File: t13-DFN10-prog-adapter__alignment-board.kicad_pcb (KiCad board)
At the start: 2 copper layers, 13.2 x 16.8 mm, 21 parts, among them P3 DFN10

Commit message: Tweaks.
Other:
- board text added: "V0.10.b"
- board text added: "X"
- board text added: "t13-DFN10 P.A."
- board text removed: "ATtiny13"
- board text removed: "DFN10"
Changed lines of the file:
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@@
-(kicad_pcb (version 3) (host pcbnew "(2014-03-16 BZR 4752)-product")
+(kicad_pcb (version 3) (host pcbnew "(2014-03-14 BZR 4750)-product")
   (general
     (links 0)
@@
     (area 139.15099 91.5068 153.96501 110.7312)
     (thickness 1.6)
-    (drawings 13)
+    (drawings 14)
     (tracks 0)
     (zones 0)
@@
   (page A4)
   (title_block
-    (title "ATtiny13 DFN10 programming adapter")
+    (title "ATtiny13 DFN10 programming adapter - alignment board")
     (date "17 Mar 2014")
-    (rev 0.10.a)
+    (rev 0.10.b)
     (company "2014 - blog.spitzenpfeil.org")
   )
@@
     (mod_text_size 1 1)
     (mod_text_width 0.15)
-    (pad_size 0.3302 0.3302)
-    (pad_drill 0.3302)
+    (pad_size 1.65 1.65)
+    (pad_drill 0.6)
     (pad_to_mask_clearance 0)
     (aux_axis_origin 0 0)
@@
       (effects (font (size 1 1) (thickness 0.2)))
     )
-    (pad 1 thru_hole rect (at 0 0) (size 1.65 1.65) (drill 0.508) (layers *.Cu *.Mask F.SilkS))
+    (pad 1 thru_hole rect (at 0 0) (size 1.65 1.65) (drill 0.6) (layers *.Cu *.Mask F.SilkS))
   )
   (module my_parts:MADW__SIL-1 (layer F.Cu)
@@
       (effects (font (size 1 1) (thickness 0.2)))
     )
-    (pad 1 thru_hole rect (at 0 0) (size 1.65 1.65) (drill 0.508) (layers *.Cu *.Mask F.SilkS))
+    (pad 1 thru_hole rect (at 0 0) (size 1.65 1.65) (drill 0.6) (layers *.Cu *.Mask F.SilkS))
   )
   (module my_parts:MADW__SIL-1 (layer F.Cu)
@@
       (effects (font (size 1 1) (thickness 0.2)))
     )
-    (pad 1 thru_hole rect (at 0 0) (size 1.65 1.65) (drill 0.508) (layers *.Cu *.Mask F.SilkS))
+    (pad 1 thru_hole rect (at 0 0) (size 1.65 1.65) (drill 0.6) (layers *.Cu *.Mask F.SilkS))
   )
   (module my_parts:MADW__SIL-1 (layer F.Cu)
@@
     (fp_line (start 1.27 -1.27) (end 1.27 1.27) (layer F.SilkS) (width 0.2))
     (fp_line (start -1.27 1.27) (end -1.27 -1.27) (layer F.SilkS) (width 0.2))
-    (pad 1 thru_hole rect (at 0 0) (size 1.65 1.65) (drill 0.508) (layers *.Cu *.Mask F.SilkS))
+    (pad 1 thru_hole rect (at 0 0) (size 1.65 1.65) (drill 0.6) (layers *.Cu *.Mask F.SilkS))
+  )
+  (gr_text X (at 146.6 101.2) (layer F.SilkS)
+    (effects (font (size 1.2 1.2) (thickness 0.3)) (justify mirror))
+  )
+  (gr_text V0.10.b (at 146.6 105.2) (layer F.SilkS)
+    (effects (font (size 1 1) (thickness 0.25)))
   )
   (gr_text 10...6 (at 146.4056 94.742) (layer F.SilkS)
@@
   (gr_line (start 153.162 92.71) (end 153.162 109.474) (angle 90) (layer Edge.Cuts) (width 0.1))
   (gr_line (start 139.954 92.71) (end 153.162 92.71) (angle 90) (layer Edge.Cuts) (width 0.1))
-  (gr_text DFN10 (at 146.5834 104.775) (layer F.SilkS)
-    (effects (font (size 1.2 1.2) (thickness 0.25)))
-  )
-  (gr_text ATtiny13 (at 146.558 97.7646) (layer F.SilkS)
-    (effects (font (size 1.2 1.2) (thickness 0.25)))
+  (gr_text "t13-DFN10 P.A." (at 146.6 97.4) (layer F.SilkS)
+    (effects (font (size 1 1) (thickness 0.25)))
   )
   (gr_line (start 140.208 92.964) (end 152.908 92.964) (angle 90) (layer F.SilkS) (width 0.2))

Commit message: Tweaks.
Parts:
- removed the P? at (145.9, 102.2)
- removed the P? at (147.2, 102.2)
- removed the P? at (146.6, 102.2)
- removed the P? at (146.6, 100.0)
- removed the P? at (147.2, 100.0)
- removed the P? at (145.9, 100.0)
- removed the P? at (145.5, 101.8)
- removed the P? at (145.5, 100.4)
- removed the P? at (145.5, 101.1)
- removed the P? at (147.7, 101.1)
- removed the P? at (147.7, 100.4)
- removed the P? at (147.7, 101.8)
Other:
- outline, holes or cut-outs redrawn
- board text removed: "X"
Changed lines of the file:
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@@
     (area 139.15099 91.5068 153.96501 110.7312)
     (thickness 1.6)
-    (drawings 14)
+    (drawings 22)
     (tracks 0)
     (zones 0)
-    (modules 21)
+    (modules 9)
     (nets 1)
   )
@@
   )
   (module my_parts:MADW__SIL-1 (layer F.Cu)
-    (at 145.4658 101.7778 90)
-    (descr "Connecteurs 2 pins")
-    (tags "CONN DEV")
-    (fp_text reference P? (at 0 -2.032 90) (layer F.SilkS) hide
-      (effects (font (size 1 1) (thickness 0.2)))
-    )
-    (fp_text value VAL** (at 0 2.286 90) (layer F.SilkS) hide
-      (effects (font (size 1 1) (thickness 0.2)))
-    )
-    (pad "" np_thru_hole circle (at 0 0 90) (size 0.3302 0.3302) (drill 0.3302) (layers *.Cu *.Mask F.SilkS))
-  )
-  (module my_parts:MADW__SIL-1 (layer F.Cu)
-    (at 145.4658 100.4062 90)
-    (descr "Connecteurs 2 pins")
-    (tags "CONN DEV")
-    (fp_text reference P? (at 0 -2.032 90) (layer F.SilkS) hide
-      (effects (font (size 1 1) (thickness 0.2)))
-    )
-    (fp_text value VAL** (at 0 2.286 90) (layer F.SilkS) hide
-      (effects (font (size 1 1) (thickness 0.2)))
-    )
-    (pad "" np_thru_hole circle (at 0 0 90) (size 0.3302 0.3302) (drill 0.3302) (layers *.Cu *.Mask F.SilkS))
-  )
-  (module my_parts:MADW__SIL-1 (layer F.Cu)
-    (at 145.4658 101.092 90)
-    (descr "Connecteurs 2 pins")
-    (tags "CONN DEV")
-    (fp_text reference P? (at 0 -2.032 90) (layer F.SilkS) hide
-      (effects (font (size 1 1) (thickness 0.2)))
-    )
-    (fp_text value VAL** (at 0 2.286 90) (layer F.SilkS) hide
-      (effects (font (size 1 1) (thickness 0.2)))
-    )
-    (pad "" np_thru_hole circle (at 0 0 90) (size 0.3302 0.3302) (drill 0.3302) (layers *.Cu *.Mask F.SilkS))
-  )
-  (module my_parts:MADW__SIL-1 (layer F.Cu)
-    (at 147.6756 101.092 90)
-    (descr "Connecteurs 2 pins")
-    (tags "CONN DEV")
-    (fp_text reference P? (at 0 -2.032 90) (layer F.SilkS) hide
-      (effects (font (size 1 1) (thickness 0.2)))
-    )
-    (fp_text value VAL** (at 0 2.286 90) (layer F.SilkS) hide
-      (effects (font (size 1 1) (thickness 0.2)))
-    )
-    (pad "" np_thru_hole circle (at 0 0 90) (size 0.3302 0.3302) (drill 0.3302) (layers *.Cu *.Mask F.SilkS))
-  )
-  (module my_parts:MADW__SIL-1 (layer F.Cu)
-    (at 147.6756 100.4062 90)
-    (descr "Connecteurs 2 pins")
-    (tags "CONN DEV")
-    (fp_text reference P? (at 0 -2.032 90) (layer F.SilkS) hide
-      (effects (font (size 1 1) (thickness 0.2)))
-    )
-    (fp_text value VAL** (at 0 2.286 90) (layer F.SilkS) hide
-      (effects (font (size 1 1) (thickness 0.2)))
-    )
-    (pad "" np_thru_hole circle (at 0 0 90) (size 0.3302 0.3302) (drill 0.3302) (layers *.Cu *.Mask F.SilkS))
-  )
-  (module my_parts:MADW__SIL-1 (layer F.Cu)
-    (at 147.6756 101.7778 90)
-    (descr "Connecteurs 2 pins")
-    (tags "CONN DEV")
-    (fp_text reference P? (at 0 -2.032 90) (layer F.SilkS) hide
-      (effects (font (size 1 1) (thickness 0.2)))
-    )
-    (fp_text value VAL** (at 0 2.286 90) (layer F.SilkS) hide
-      (effects (font (size 1 1) (thickness 0.2)))
-    )
-    (pad "" np_thru_hole circle (at 0 0 90) (size 0.3302 0.3302) (drill 0.3302) (layers *.Cu *.Mask F.SilkS))
-  )
-  (module my_parts:MADW__SIL-1 (layer F.Cu)
-    (at 145.8722 102.2096)
-    (descr "Connecteurs 2 pins")
-    (tags "CONN DEV")
-    (fp_text reference P? (at 0 -2.032) (layer F.SilkS) hide
-      (effects (font (size 1 1) (thickness 0.2)))
-    )
-    (fp_text value VAL** (at 0 2.286) (layer F.SilkS) hide
-      (effects (font (size 1 1) (thickness 0.2)))
-    )
-    (pad "" np_thru_hole circle (at 0 0) (size 0.3302 0.3302) (drill 0.3302) (layers *.Cu *.Mask F.SilkS))
-  )
-  (module my_parts:MADW__SIL-1 (layer F.Cu)
-    (at 147.2438 102.2096)
-    (descr "Connecteurs 2 pins")
-    (tags "CONN DEV")
-    (fp_text reference P? (at 0 -2.032) (layer F.SilkS) hide
-      (effects (font (size 1 1) (thickness 0.2)))
-    )
-    (fp_text value VAL** (at 0 2.286) (layer F.SilkS) hide
-      (effects (font (size 1 1) (thickness 0.2)))
-    )
-    (pad "" np_thru_hole circle (at 0 0) (size 0.3302 0.3302) (drill 0.3302) (layers *.Cu *.Mask F.SilkS))
-  )
-  (module my_parts:MADW__SIL-1 (layer F.Cu)
-    (at 146.558 102.2096)
-    (descr "Connecteurs 2 pins")
-    (tags "CONN DEV")
-    (fp_text reference P? (at 0 -2.032) (layer F.SilkS) hide
-      (effects (font (size 1 1) (thickness 0.2)))
-    )
-    (fp_text value VAL** (at 0 2.286) (layer F.SilkS) hide
-      (effects (font (size 1 1) (thickness 0.2)))
-    )
-    (pad "" np_thru_hole circle (at 0 0) (size 0.3302 0.3302) (drill 0.3302) (layers *.Cu *.Mask F.SilkS))
-  )
-  (module my_parts:MADW__SIL-1 (layer F.Cu)
-    (at 146.558 99.9744)
-    (descr "Connecteurs 2 pins")
-    (tags "CONN DEV")
-    (fp_text reference P? (at 0 -2.032) (layer F.SilkS) hide
-      (effects (font (size 1 1) (thickness 0.2)))
-    )
-    (fp_text value VAL** (at 0 2.286) (layer F.SilkS) hide
-      (effects (font (size 1 1) (thickness 0.2)))
-    )
-    (pad "" np_thru_hole circle (at 0 0) (size 0.3302 0.3302) (drill 0.3302) (layers *.Cu *.Mask F.SilkS))
-  )
-  (module my_parts:MADW__SIL-1 (layer F.Cu)
-    (at 147.2438 99.9744)
-    (descr "Connecteurs 2 pins")
-    (tags "CONN DEV")
-    (fp_text reference P? (at 0 -2.032) (layer F.SilkS) hide
-      (effects (font (size 1 1) (thickness 0.2)))
-    )
-    (fp_text value VAL** (at 0 2.286) (layer F.SilkS) hide
-      (effects (font (size 1 1) (thickness 0.2)))
-    )
-    (pad "" np_thru_hole circle (at 0 0) (size 0.3302 0.3302) (drill 0.3302) (layers *.Cu *.Mask F.SilkS))
-  )
-  (module my_parts:MADW__SIL-1 (layer F.Cu)
-    (at 145.8722 99.9744)
-    (descr "Connecteurs 2 pins")
-    (tags "CONN DEV")
-    (fp_text reference P? (at 0 -2.032) (layer F.SilkS) hide
-      (effects (font (size 1 1) (thickness 0.2)))
-    )
-    (fp_text value VAL** (at 0 2.286) (layer F.SilkS) hide
-      (effects (font (size 1 1) (thickness 0.2)))
-    )
-    (pad "" np_thru_hole circle (at 0 0) (size 0.3302 0.3302) (drill 0.3302) (layers *.Cu *.Mask F.SilkS))
-  )
-  (module my_parts:MADW__SIL-1 (layer F.Cu)
     (at 145.0594 102.5906)
     (descr "Connecteurs 2 pins")
@@
     (pad 1 thru_hole rect (at 0 0) (size 1.65 1.65) (drill 0.6) (layers *.Cu *.Mask F.SilkS))
   )
-  (gr_text X (at 146.6 101.2) (layer F.SilkS)
-    (effects (font (size 1.2 1.2) (thickness 0.3)) (justify mirror))
-  )
+  (gr_line (start 145.2118 101.0158) (end 145.2118 101.1682) (angle 90) (layer Edge.Cuts) (width 0.1))
+  (gr_line (start 146.4818 102.4382) (end 146.6342 102.4382) (angle 90) (layer Edge.Cuts) (width 0.1))
+  (gr_line (start 147.9042 101.0158) (end 147.9042 101.1682) (angle 90) (layer Edge.Cuts) (width 0.1))
+  (gr_line (start 146.4818 99.7458) (end 146.6342 99.7458) (angle 90) (layer Edge.Cuts) (width 0.1))
+  (gr_arc (start 146.4818 101.1682) (end 146.4818 102.4382) (angle 90) (layer Edge.Cuts) (width 0.1))
+  (gr_arc (start 146.6342 101.1682) (end 147.9042 101.1682) (angle 90) (layer Edge.Cuts) (width 0.1))
+  (gr_arc (start 146.6342 101.0158) (end 146.6342 99.7458) (angle 90) (layer Edge.Cuts) (width 0.1))
+  (gr_arc (start 146.4818 101.0158) (end 145.2118 101.0158) (angle 90) (layer Edge.Cuts) (width 0.1))
+  (gr_line (start 148.0566 99.5934) (end 148.0566 99.568) (angle 90) (layer Eco1.User) (width 0.2))
   (gr_text V0.10.b (at 146.6 105.2) (layer F.SilkS)
     (effects (font (size 1 1) (thickness 0.25)))

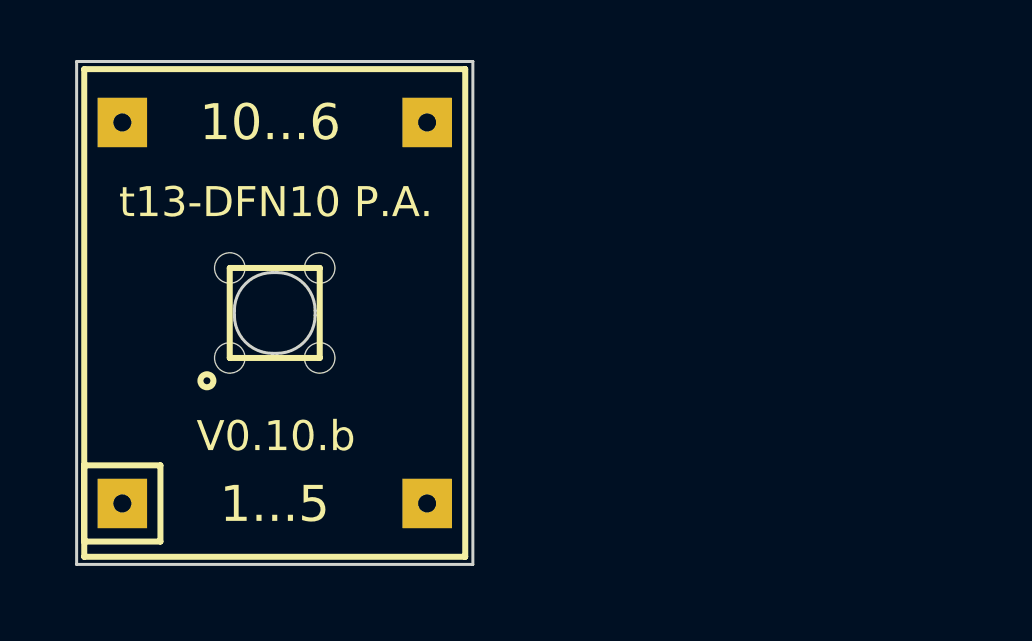
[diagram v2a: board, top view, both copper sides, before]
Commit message: Added a routing layer.
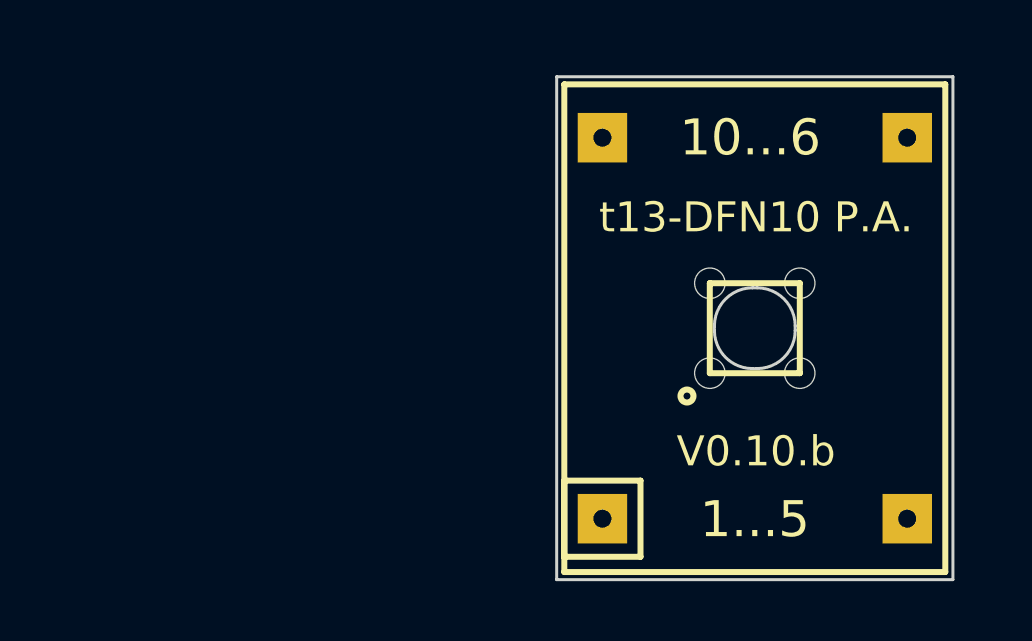
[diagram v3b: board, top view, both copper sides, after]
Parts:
- moved P3 16.0 mm to (162.6, 101.6)
- moved P? 16.0 mm to (164.1, 103.1)
- moved P? 16.0 mm to (164.1, 100.1)
- moved P? 16.0 mm to (167.6, 108.0)
- moved P? 16.0 mm to (167.6, 95.2)
- moved P? 16.0 mm to (157.5, 95.2)
- moved P? 16.0 mm to (161.1, 103.1)
- moved P? 16.0 mm to (161.1, 100.1)
- moved P? 16.0 mm to (157.5, 108.0)

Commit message: Got the prototypes, adjusted internal cutouts.
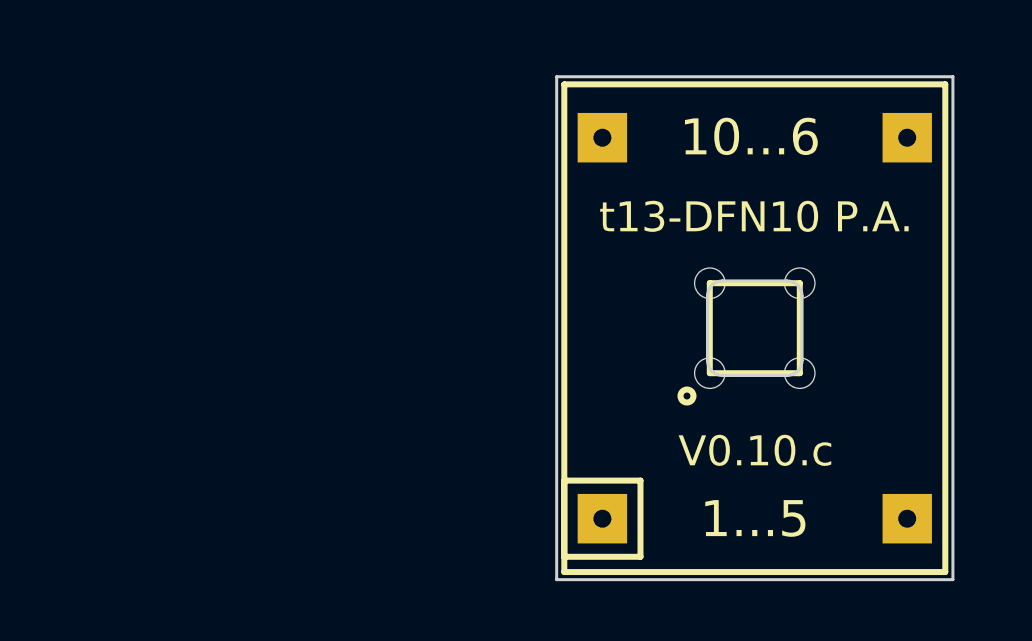
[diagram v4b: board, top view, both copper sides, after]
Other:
- outline, holes or cut-outs redrawn
- board text added: "* routing bit: 1.00mm * routed out to center of the line"
- board text added: "V0.10.c"
- board text removed: "V0.10.b"
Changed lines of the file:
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@@
-(kicad_pcb (version 3) (host pcbnew "(2014-03-14 BZR 4750)-product")
+(kicad_pcb (version 3) (host pcbnew "(2014-04-04 BZR 4786)-product")
   (general
     (links 0)
     (no_connects 0)
-    (area 155.15299 92.0148 169.96701 111.2392)
+    (area 153.67 92.0148 179.722388 122.38)
     (thickness 1.6)
-    (drawings 25)
+    (drawings 23)
     (tracks 0)
     (zones 0)
@@
     (0 B.Cu signal)
     (20 B.SilkS user)
-    (21 F.SilkS user)
+    (21 F.SilkS user hide)
     (22 B.Mask user)
     (23 F.Mask user)
@@
     (zone_45_only no)
     (trace_min 0.254)
-    (segment_width 0.2)
+    (segment_width 0.1)
     (edge_width 0.1)
     (via_size 0.889)
@@
     (mod_text_size 1 1)
     (mod_text_width 0.15)
-    (pad_size 1.65 1.65)
-    (pad_drill 0.6)
+    (pad_size 1.016 1.016)
+    (pad_drill 1.016)
     (pad_to_mask_clearance 0)
     (aux_axis_origin 0 0)
@@
     (pad 1 thru_hole rect (at 0 0) (size 1.65 1.65) (drill 0.6) (layers *.Cu *.Mask F.SilkS))
   )
-  (gr_line (start 161.06 103.1) (end 161.06 100.1) (angle 90) (layer Eco1.User) (width 0.1))
-  (gr_line (start 164.06 103.1) (end 161.06 103.1) (angle 90) (layer Eco1.User) (width 0.1))
-  (gr_line (start 164.06 100.1) (end 164.06 103.1) (angle 90) (layer Eco1.User) (width 0.1))
-  (gr_line (start 161.06 100.1) (end 164.06 100.1) (angle 90) (layer Eco1.User) (width 0.1))
-  (gr_line (start 161.2138 101.5238) (end 161.2138 101.6762) (angle 90) (layer Edge.Cuts) (width 0.1))
-  (gr_line (start 162.4838 102.9462) (end 162.6362 102.9462) (angle 90) (layer Edge.Cuts) (width 0.1))
-  (gr_line (start 163.9062 101.5238) (end 163.9062 101.6762) (angle 90) (layer Edge.Cuts) (width 0.1))
-  (gr_line (start 162.4838 100.2538) (end 162.6362 100.2538) (angle 90) (layer Edge.Cuts) (width 0.1))
-  (gr_arc (start 162.4838 101.6762) (end 162.4838 102.9462) (angle 90) (layer Edge.Cuts) (width 0.1))
-  (gr_arc (start 162.6362 101.6762) (end 163.9062 101.6762) (angle 90) (layer Edge.Cuts) (width 0.1))
-  (gr_arc (start 162.6362 101.5238) (end 162.6362 100.2538) (angle 90) (layer Edge.Cuts) (width 0.1))
-  (gr_arc (start 162.4838 101.5238) (end 161.2138 101.5238) (angle 90) (layer Edge.Cuts) (width 0.1))
-  (gr_text V0.10.b (at 162.602 105.708) (layer F.SilkS)
+  (gr_line (start 161.485 103.175) (end 163.635 103.175) (angle 90) (layer Edge.Cuts) (width 0.1))
+  (gr_line (start 160.985 100.525) (end 160.985 102.675) (angle 90) (layer Edge.Cuts) (width 0.1))
+  (gr_line (start 163.635 100.025) (end 161.485 100.025) (angle 90) (layer Edge.Cuts) (width 0.1))
+  (gr_line (start 164.135 102.675) (end 164.135 100.525) (angle 90) (layer Edge.Cuts) (width 0.1))
+  (gr_arc (start 163.635 102.675) (end 164.135 102.675) (angle 90) (layer Edge.Cuts) (width 0.1))
+  (gr_arc (start 161.485 102.675) (end 161.485 103.175) (angle 90) (layer Edge.Cuts) (width 0.1))
+  (gr_arc (start 161.485 100.525) (end 160.985 100.525) (angle 90) (layer Edge.Cuts) (width 0.1))
+  (gr_arc (start 163.635 100.525) (end 163.635 100.025) (angle 90) (layer Edge.Cuts) (width 0.1))
+  (gr_line (start 161.485 103.175) (end 163.635 103.175) (angle 90) (layer Eco1.User) (width 0.1))
+  (gr_line (start 160.985 100.525) (end 160.985 102.675) (angle 90) (layer Eco1.User) (width 0.1))
+  (gr_line (start 163.635 100.025) (end 161.485 100.025) (angle 90) (layer Eco1.User) (width 0.1))
+  (gr_line (start 164.135 102.675) (end 164.135 100.525) (angle 90) (layer Eco1.User) (width 0.1))
+  (gr_arc (start 163.635 102.675) (end 164.135 102.675) (angle 90) (layer Eco1.User) (width 0.1))
+  (gr_arc (start 161.485 102.675) (end 161.485 103.175) (angle 90) (layer Eco1.User) (width 0.1))
+  (gr_arc (start 161.485 100.525) (end 160.985 100.525) (angle 90) (layer Eco1.User) (width 0.1))
+  (gr_arc (start 163.635 100.525) (end 163.635 100.025) (angle 90) (layer Eco1.User) (width 0.1))
+  (dimension 3.15 (width 0.1) (layer Eco1.User)
+    (gr_text "3.150 mm" (at 162.71 117.295) (layer Eco1.User)
+      (effects (font (size 1 1) (thickness 0.1)))
+    )
+    (feature1 (pts (xy 164.135 103.325) (xy 164.135 116.135)))
+    (feature2 (pts (xy 160.985 103.325) (xy 160.985 116.135)))
+    (crossbar (pts (xy 160.985 113.435) (xy 164.135 113.435)))
+    (arrow1a (pts (xy 164.135 113.435) (xy 163.008496 114.021421)))
+    (arrow1b (pts (xy 164.135 113.435) (xy 163.008496 112.848579)))
+    (arrow2a (pts (xy 160.985 113.435) (xy 162.111504 114.021421)))
+    (arrow2b (pts (xy 160.985 113.435) (xy 162.111504 112.848579)))
+  )
+  (gr_text "* routing bit: 1.00mm\n* routed out to center of the line" (at 153.72 120.88) (layer Eco1.User)
+    (effects (font (size 1 1) (thickness 0.1)) (justify left))
+  )
+  (gr_text V0.10.c (at 162.602 105.708) (layer F.SilkS)
     (effects (font (size 1 1) (thickness 0.25)))
   )
